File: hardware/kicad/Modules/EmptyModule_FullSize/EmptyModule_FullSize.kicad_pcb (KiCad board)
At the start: 2 copper layers, 38 x 64 mm, 2 parts, among them J1 Conn_02x04_Odd_Even, J2 Conn_02x04_Odd_Even

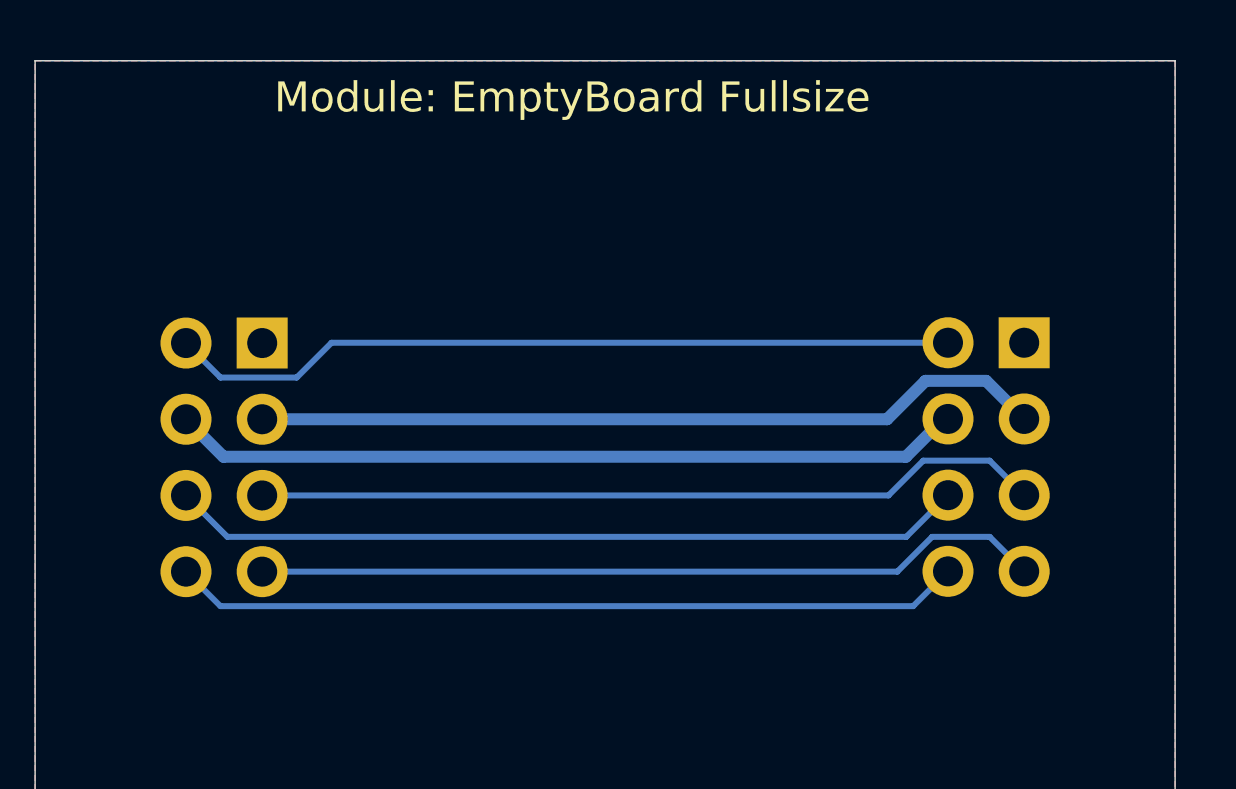
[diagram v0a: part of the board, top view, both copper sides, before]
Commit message: feat(hardware): update FullSize empty module template
- update schematic and PCB from the daughterboard design block
- preserve linked design block groups and connector references
- correct connector alignment and power routing widths
- remove duplicate same-net routing
- validate pinout, geometry, ERC, and DRC
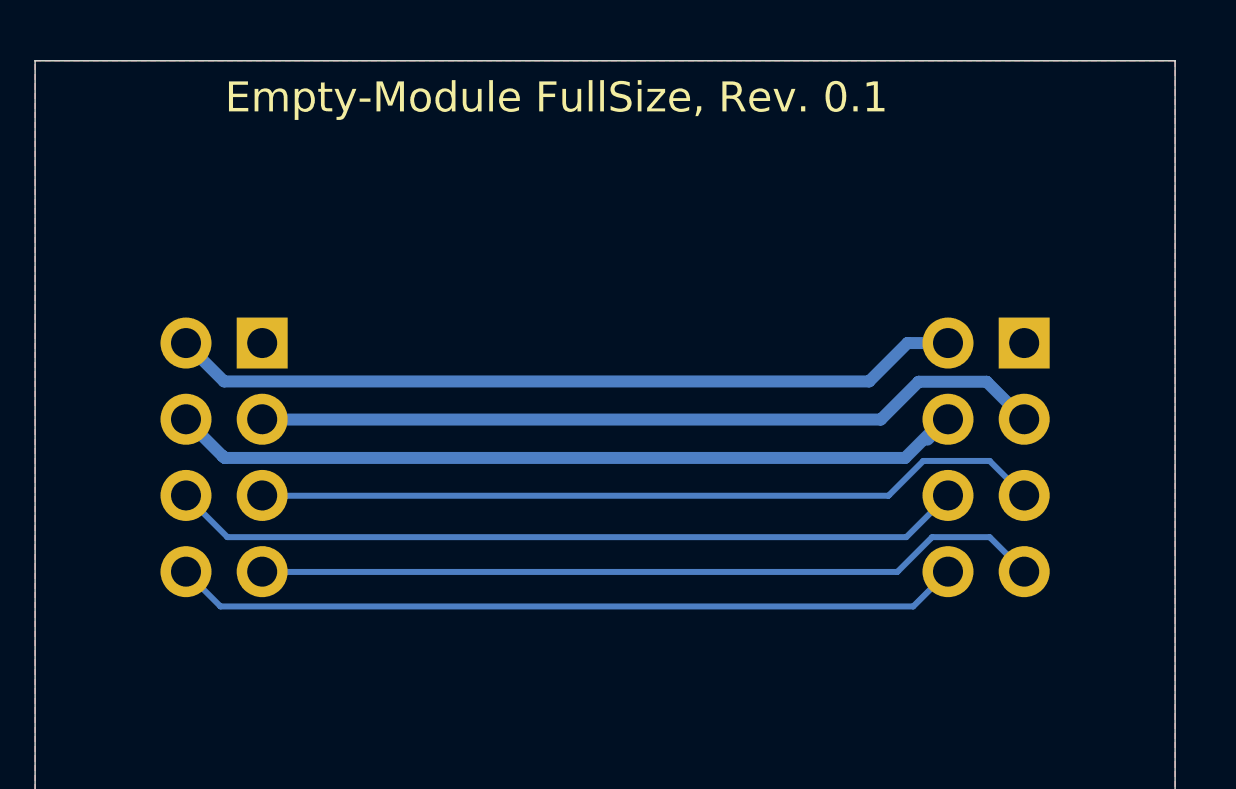
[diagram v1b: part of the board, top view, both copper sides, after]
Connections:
- net 24V renamed /24V
- net 3V3 renamed /3V3
- net 5V renamed /5V
- net GND renamed /GND
- net GPIO1 renamed /GPIO1
- net GPIO2 renamed /GPIO2
- net SCL renamed /SCL
- net SDA renamed /SDA
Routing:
- net /5V: track 26.4 -> 27.4 mm
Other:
- board text added: "${TITLE}, Rev. ${REVISION}"
- board text removed: "Module: EmptyBoard Fullsize"
